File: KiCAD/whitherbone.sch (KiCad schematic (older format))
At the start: 51 parts, among them SW1 POWER, U1 OSD3358-512M-BSM, U2 SN74LVC1G07DCK, U3 TPD4S012DRY, X1 10118192-0001LF, X2 MICROSD, Y1 24 MHz

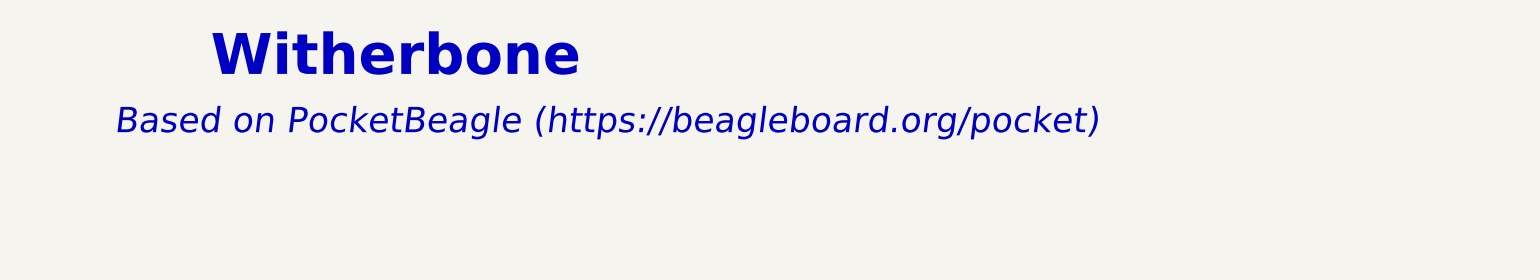
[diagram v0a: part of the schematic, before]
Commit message: Make sure name is whitherbone everywhere
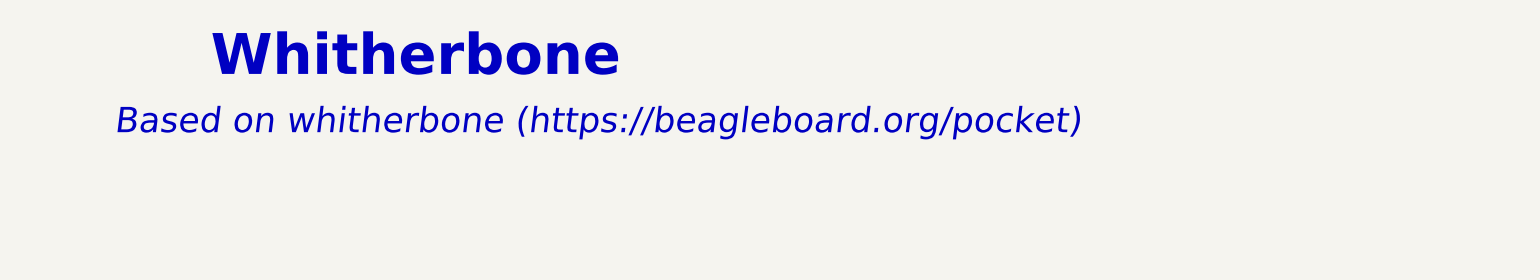
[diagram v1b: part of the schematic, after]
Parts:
- C1, C2, C3, C4, C5, C7, R1, R12, R2, R3: footprint PocketBeagle.pretty:0402 -> whitherbone.pretty:0402
- C6, FB1, FB2: footprint PocketBeagle.pretty:0603 -> whitherbone.pretty:0603
- FUD1, FUD2, FUD3: footprint PocketBeagle.pretty:FIDUCIAL_40MIL -> whitherbone.pretty:FIDUCIAL_40MIL
- LED1, USR0, USR1, USR2, USR3: footprint PocketBeagle.pretty:0603-LED -> whitherbone.pretty:0603-LED
- P1, P2: footprint PocketBeagle.pretty:TH-2X18-(35MIL-DIA)-W_O-SILK -> whitherbone.pretty:TH-2X18-(35MIL-DIA)-W_O-SILK
- R10, R11, R4, R5, R6, R7, R8, R9: footprint PocketBeagle.pretty:RN0804 -> whitherbone.pretty:RN0804
- SW1: footprint PocketBeagle.pretty:MINI_PUSHBUTTON -> whitherbone.pretty:MINI_PUSHBUTTON
- TP1, TP10, TP11, TP12, TP2, TP3, TP4, TP5, TP6, TP7, TP8, TP9: footprint PocketBeagle.pretty:B1_27 -> whitherbone.pretty:B1_27
- U1: footprint PocketBeagle.pretty:OSD335X-BGA-256 -> whitherbone.pretty:OSD335X-BGA-256
- U2: footprint PocketBeagle.pretty:SC70(TI-DCK) -> whitherbone.pretty:SC70(TI-DCK)
- U3: footprint PocketBeagle.pretty:SON-6(TI)-DRY -> whitherbone.pretty:SON-6(TI)-DRY
- X1: footprint PocketBeagle.pretty:10118192-0001LF(MICRO-USB-B-AMPHENOL-FCI) -> whitherbone.pretty:10118192-0001LF(MICRO-USB-B-AMPHENOL-FCI)
- X2: footprint PocketBeagle.pretty:MICROSD -> whitherbone.pretty:MICROSD
- Y1: footprint PocketBeagle.pretty:CRYSTAL_5X3.2MM -> whitherbone.pretty:CRYSTAL_5X3.2MM
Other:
- note added: "Based on whitherbone (https://beagleboard.org/pocket)"
- note added: "Whitherbone\n"
- note removed: "Based on PocketBeagle (https://beagleboard.org/pocket)"
- note removed: "Witherbone\n"

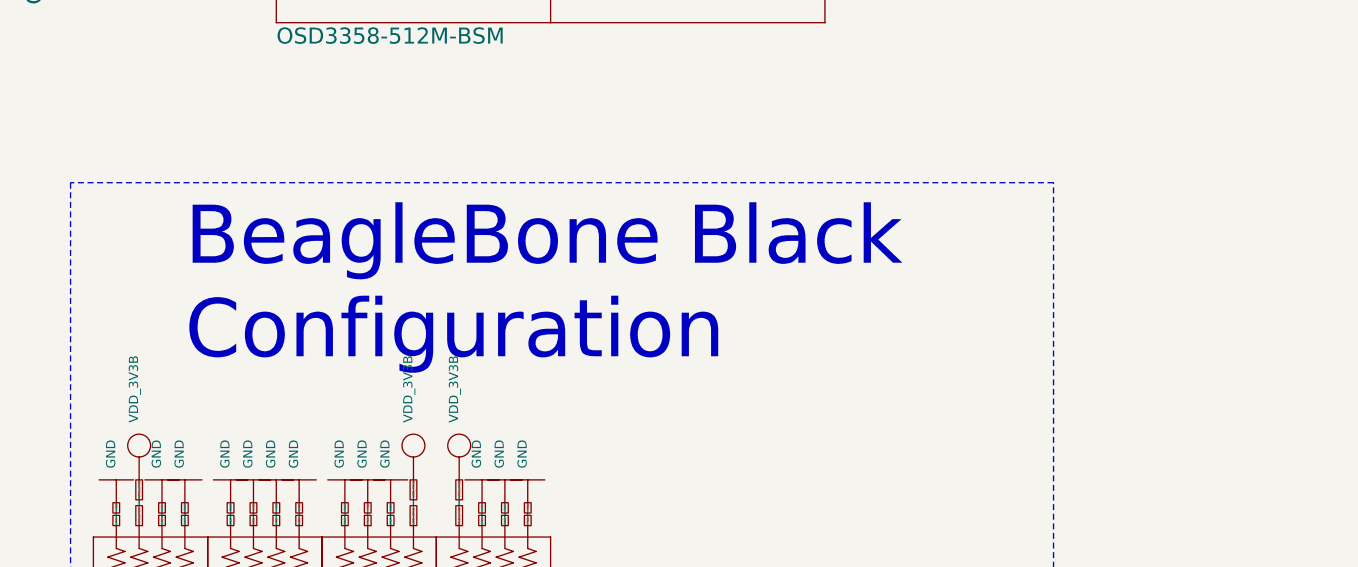
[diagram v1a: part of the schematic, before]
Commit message: SCH: label boot configuration
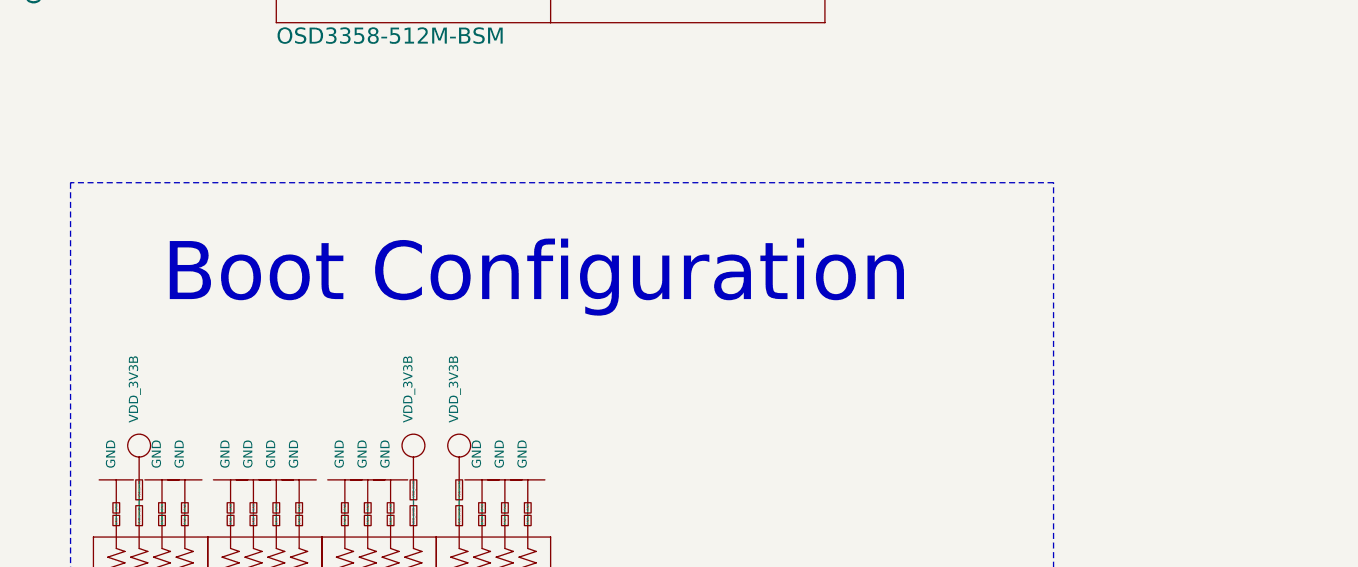
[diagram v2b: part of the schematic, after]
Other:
- note added: "Boot Configuration"
- note removed: "BeagleBone Black\nConfiguration"
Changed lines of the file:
@@
 Text Notes 21050 11350 0    254  ~ 0
 USB Device
-Text Notes 4650 10800 0    254  ~ 0
-BeagleBone Black\nConfiguration
+Text Notes 4550 10550 0    254  ~ 0
+Boot Configuration
 Text Notes 25400 11500 0    254  ~ 0
 USER LEDs

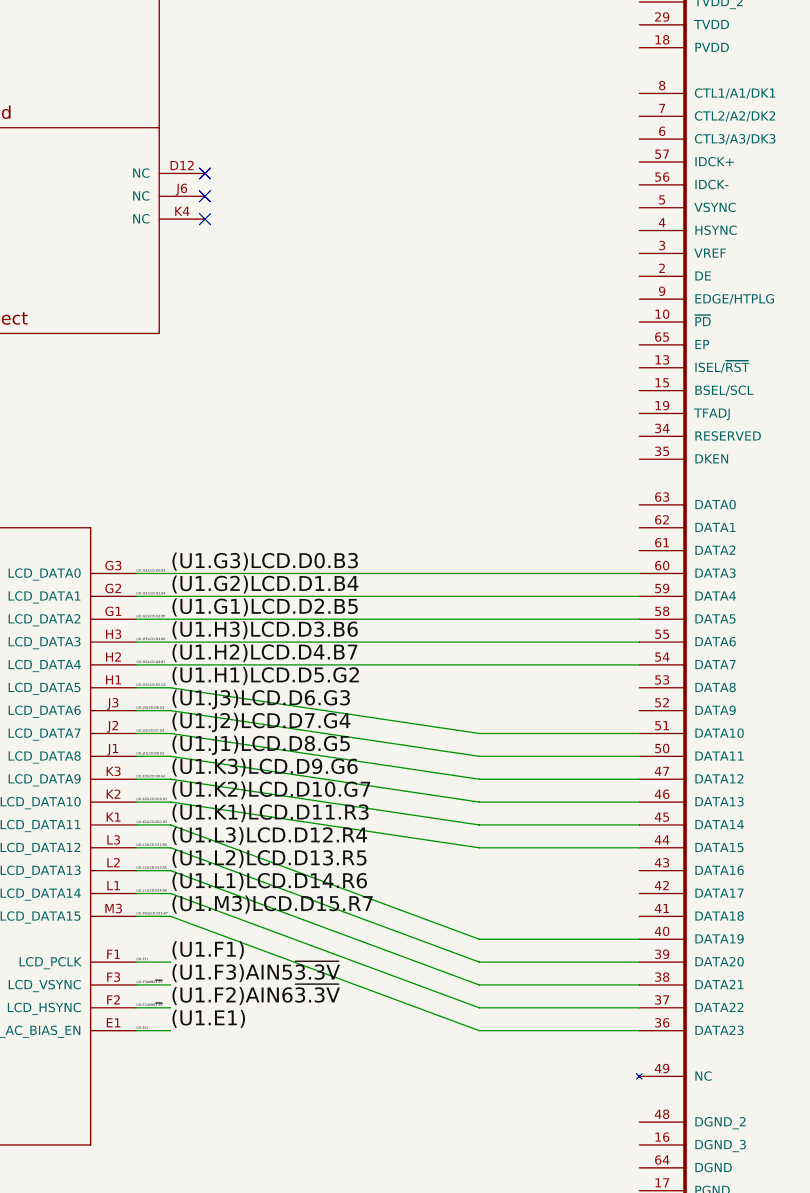
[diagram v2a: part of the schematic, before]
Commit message: Start EAGLE version based on BeagleBone Black Wireless
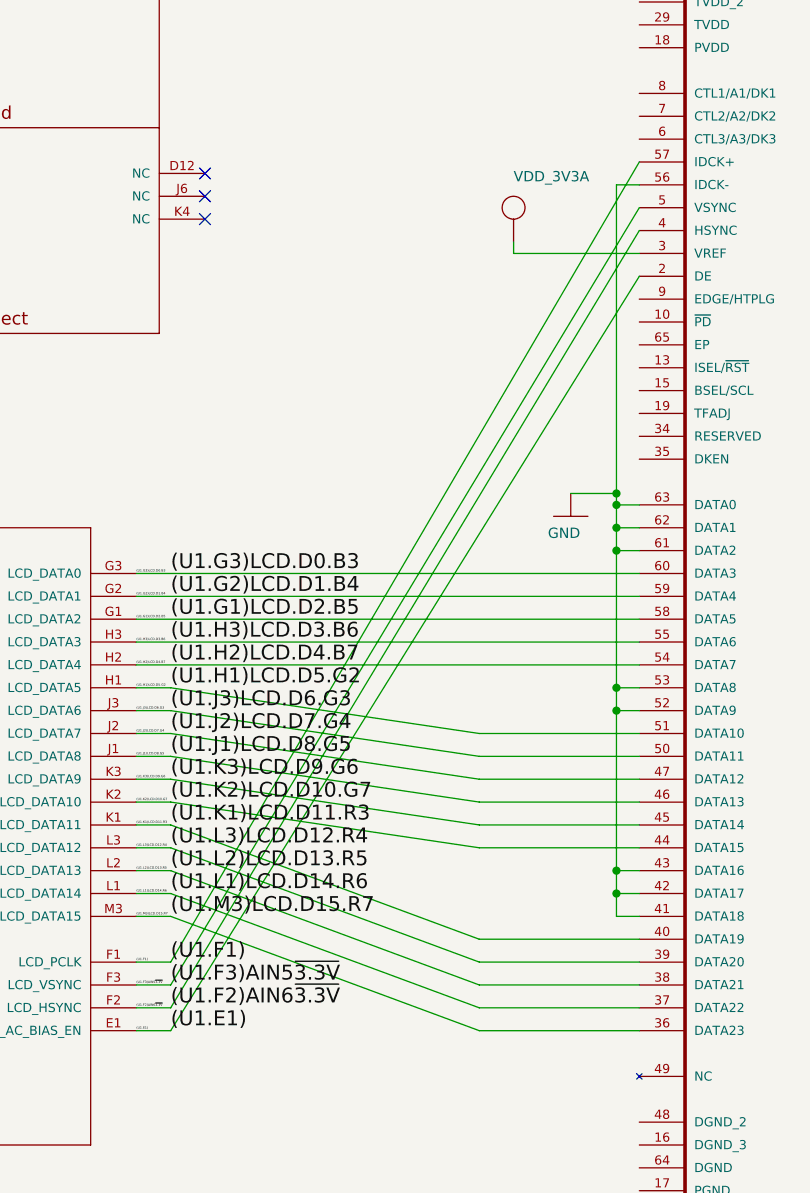
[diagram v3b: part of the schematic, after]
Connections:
- net (U1.E1): now also U?.2 (DE)
- net (U1.F1): now also U?.57 (IDCK+)
- net (U1.F2)AIN6~3.3V: now also U?.4 (HSYNC)
- net (U1.F3)AIN5~3.3V: now also U?.5 (VSYNC)
- net GND: now also U?.41 (DATA18), U?.42 (DATA17), U?.43 (DATA16), U?.52 (DATA9), U?.53 (DATA8), U?.56 (IDCK-), U?.61 (DATA2), U?.62 (DATA1), U?.63 (DATA0)
- net VDD_3V3A: now also U?.3 (VREF)
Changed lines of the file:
@@
 Wire Wire Line
 	15050 18800 16400 19300
+Wire Wire Line
+	15050 19400 17100 15900
+Wire Wire Line
+	15050 19500 17100 16100
+Wire Wire Line
+	15050 19600 17100 16200
+Wire Wire Line
+	15050 19700 17100 16400
+$Comp
+L GND #GND?
+U 1 1 5A4EE95B
+P 16800 17450
+F 0 "#GND?" H 16800 17450 45  0001 L BNN
+F 1 "GND" H 16700 17350 45  0000 L BNN
+F 2 "" H 16800 17450 60  0001 C CNN
+F 3 "" H 16800 17450 60  0001 C CNN
+	1    16800 17450
+	1    0    0    -1
+$EndComp
+Wire Wire Line
+	16800 17350 17000 17350
+Wire Wire Line
+	17000 16000 17000 19200
+Wire Wire Line
+	17000 17400 17100 17400
+Wire Wire Line
+	17000 17500 17100 17500
+Connection ~ 17000 17400
+Wire Wire Line
+	17000 17600 17100 17600
+Connection ~ 17000 17500
+Wire Wire Line
+	17000 18200 17100 18200
+Connection ~ 17000 17600
+Wire Wire Line
+	17000 18300 17100 18300
+Connection ~ 17000 18200
+Wire Wire Line
+	17000 19000 17100 19000
+Connection ~ 17000 18300
+Wire Wire Line
+	17000 19100 17100 19100
+Connection ~ 17000 19000
+Wire Wire Line
+	17000 19200 17100 19200
+Connection ~ 17000 19100
+Wire Wire Line
+	17100 16000 17000 16000
+Connection ~ 17000 17350
+$Comp
+L VDD_3V3A #SUPPLY?
+U 1 1 5A4F106B
+P 16550 16150
+F 0 "#SUPPLY?" H 16550 16150 45  0001 L BNN
+F 1 "VDD_3V3A" H 16550 16310 45  0000 L BNN
+F 2 "" H 16550 16150 60  0001 C CNN
+F 3 "" H 16550 16150 60  0001 C CNN
+	1    16550 16150
+	1    0    0    -1
+$EndComp
+Wire Wire Line
+	16550 16250 16550 16300
+Wire Wire Line
+	16550 16300 17100 16300
 $EndSCHEMATC
